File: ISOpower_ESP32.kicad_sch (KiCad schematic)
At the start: 23 parts, among them J10 ESPpin1-4, J2 SDI/SDO, J4 ESP-gpio-B, J5 1-pin-edge-touch-XL, J6 Touch Pins, J7 DAC/ADC, J9 i2c-header, U2 AMS1117-3.3, U3 ESP32-WROOM-32

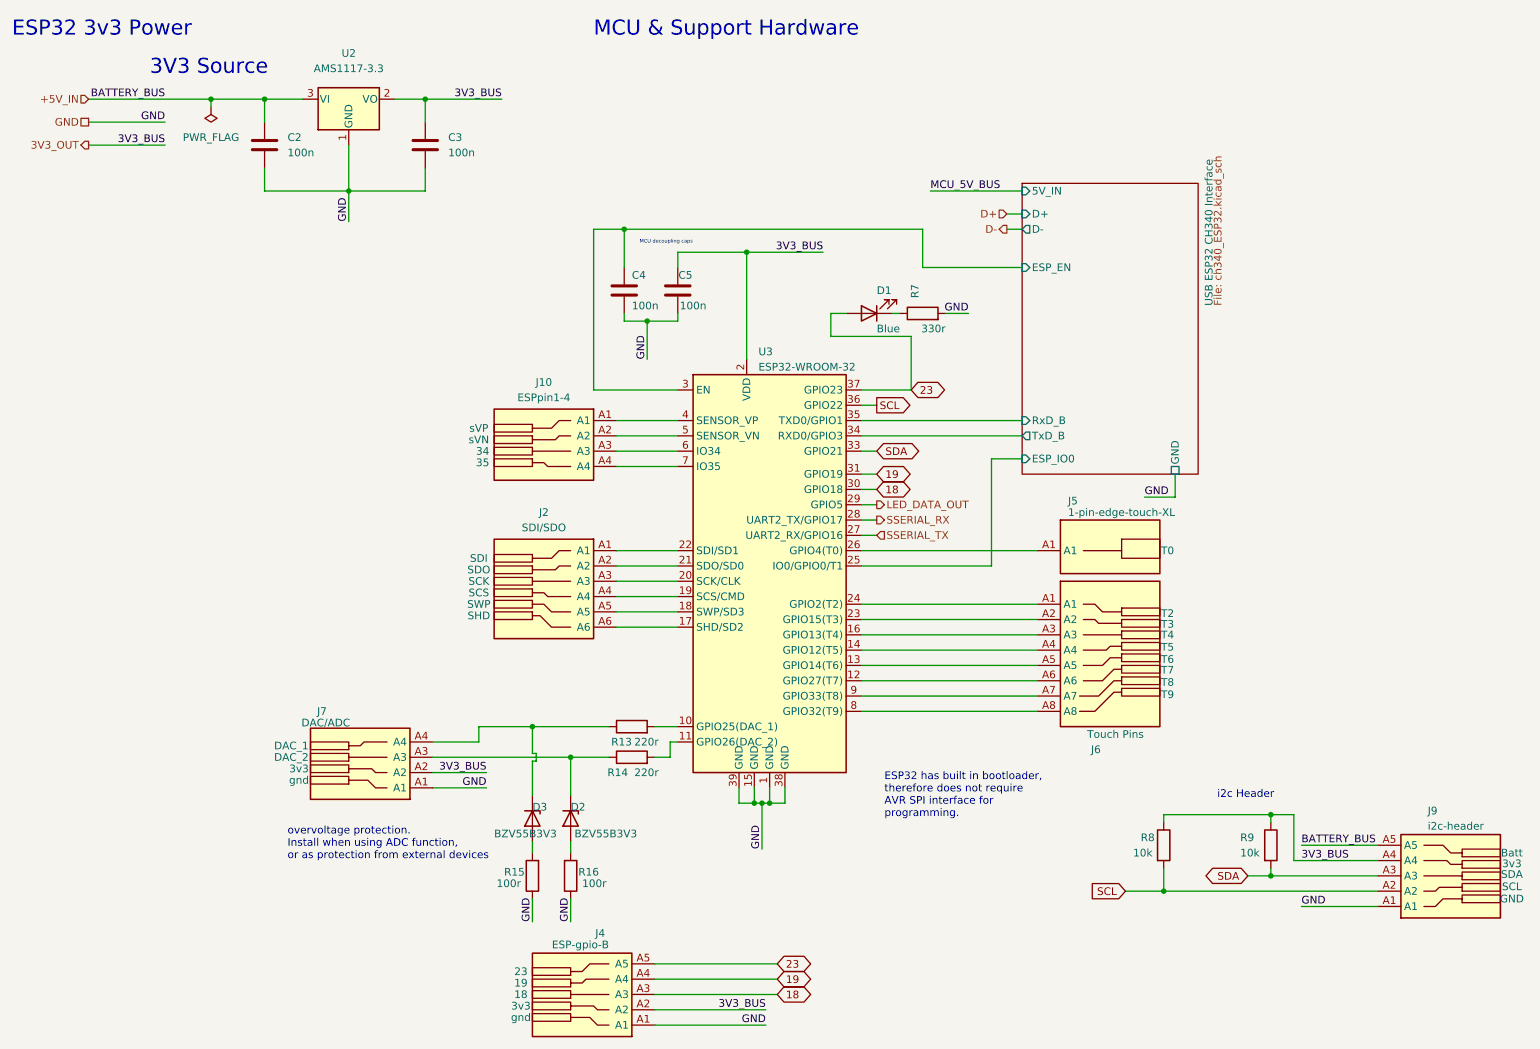
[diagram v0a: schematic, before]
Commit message: Got to Routing. Keeps crashing on me
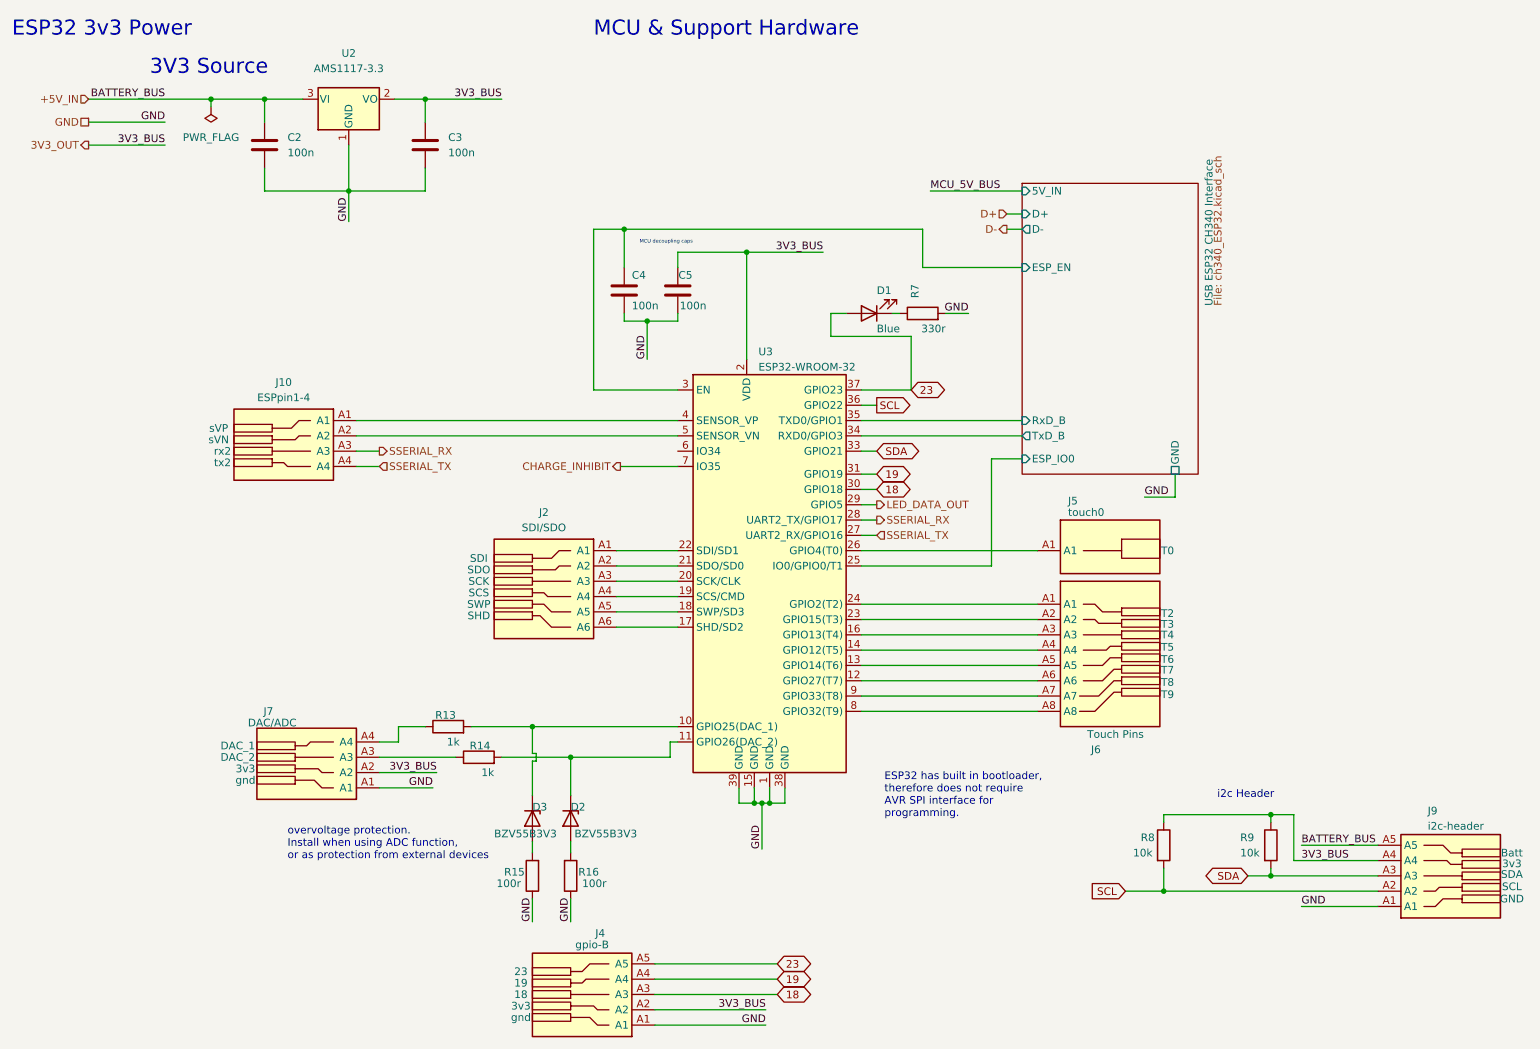
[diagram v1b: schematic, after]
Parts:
- J10: PIN3 34 -> rx2; PIN4 35 -> tx2
- J4: value ESP-gpio-B -> gpio-B
- J5: value 1-pin-edge-touch-XL -> touch0
- R13, R14: value 220r -> 1k
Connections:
- net SSERIAL_RX: now also J10.A3
- net SSERIAL_TX: now also J10.A4
- net at J7.A3, R14.1: no longer D2.1 (K)
- net at R13.2, U3.10 (GPIO25(DAC_1)): now also D3.1 (K)
- net at R14.2, U3.11 (GPIO26(DAC_2)): now also D2.1 (K)
- net at U3.6 (IO34): no longer J10.A3
- net CHARGE_INHIBIT: now reaches U3.7 (IO35)
- net CHARGE_INHIBIT: no longer J10.A4
- net at J7.A4, R13.1: no longer D3.1 (K)
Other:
- moved on the sheet: J10, J7, R13, R14

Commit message: Recoverd
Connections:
- net CHARGE_STATUS: now reaches U3.6 (IO34)
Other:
- note added: "#TODO: check voltage on these pins a and also function!"
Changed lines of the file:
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@@
     (stroke (width 0) (type default))
   )
-  (wire (pts (xy 116.205 88.9) (xy 125.73 88.9))
+  (wire (pts (xy 116.84 88.9) (xy 125.73 88.9))
     (stroke (width 0) (type default))
   )
@@
   )
   (wire (pts (xy 224.155 147.955) (xy 224.155 146.685))
+    (stroke (width 0) (type default))
+  )
+  (wire (pts (xy 116.84 86.36) (xy 125.73 86.36))
     (stroke (width 0) (type default))
   )
@@
     (effects (font (size 1.27 1.27)) (justify left bottom))
   )
+  (text "#TODO: check voltage on these pins a\nand also function!"
+    (at 86.36 95.25 0)
+    (effects (font (size 1.27 1.27)) (justify left bottom))
+  )
   (text "3V3 Source" (at 38.1 24.13 0)
     (effects (font (size 2.5 2.5)) (justify left bottom))
@@
     (effects (font (size 1.27 1.27)) (justify left))
   )
-  (hierarchical_label "CHARGE_INHIBIT" (shape output) (at 116.205 88.9 180) (fields_autoplaced)
+  (hierarchical_label "CHARGE_INHIBIT" (shape output) (at 116.84 88.9 180) (fields_autoplaced)
     (effects (font (size 1.27 1.27)) (justify right))
   )
@@
     (effects (font (size 1.27 1.27)) (justify right))
   )
+  (hierarchical_label "CHARGE_STATUS" (shape input) (at 116.84 86.36 180) (fields_autoplaced)
+    (effects (font (size 1.27 1.27)) (justify right))
+  )

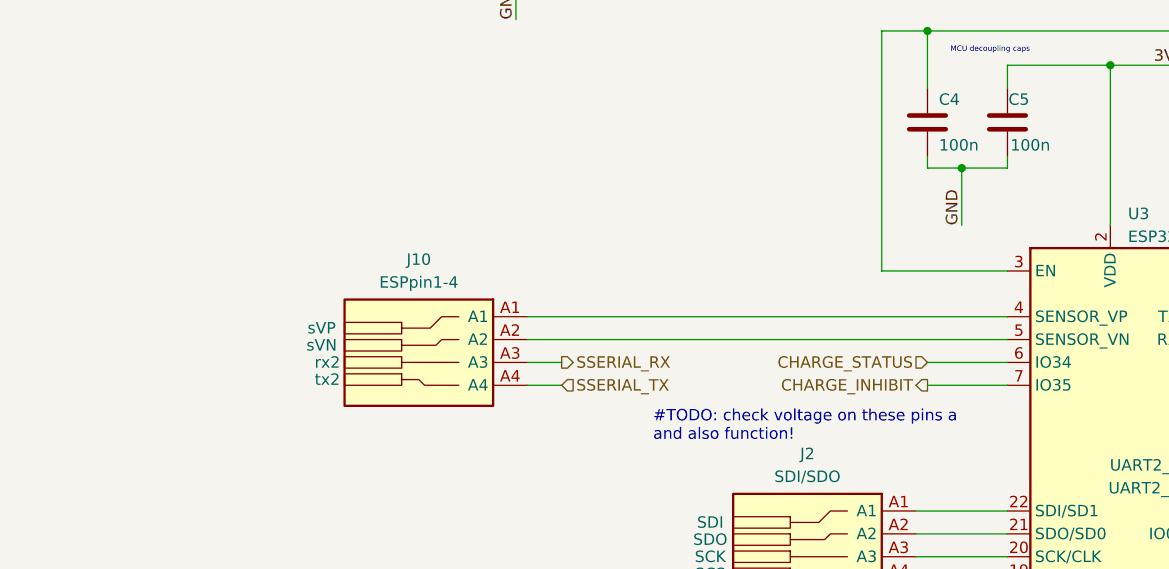
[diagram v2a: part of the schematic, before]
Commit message: Updated Schematic for Battery Charge Sense + read datasheet for battery charger IC
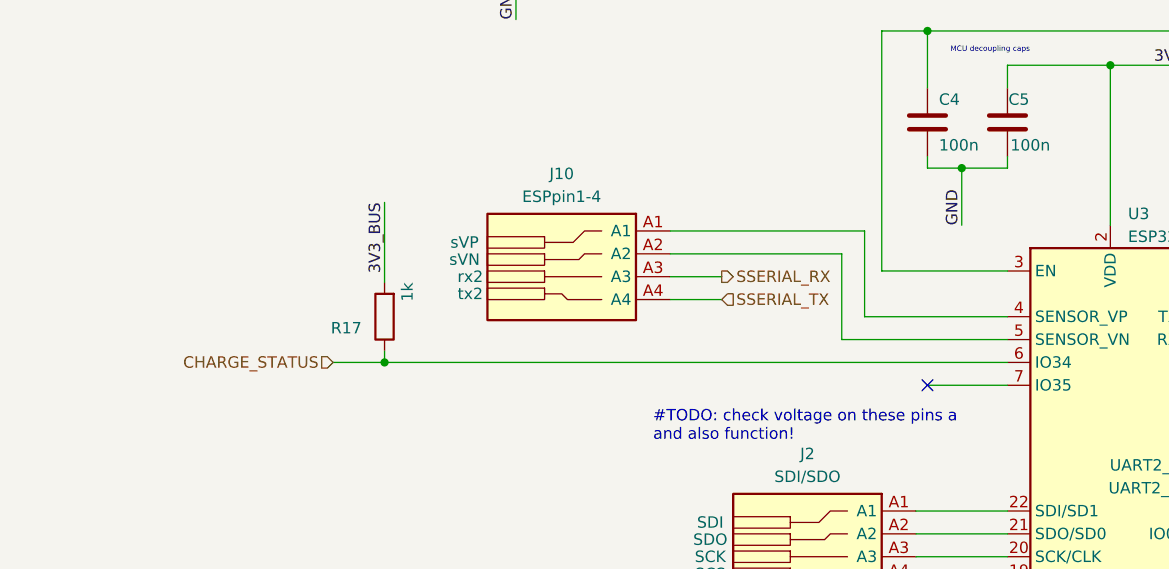
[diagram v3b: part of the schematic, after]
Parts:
- added R17: 1k, Resistor_SMD:R_0805_2012Metric_Pad1.20x1.40mm_HandSolder, symbol 000_Resistors_Immo:Resistor_0805
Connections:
- net 3V3_OUT: now also R17.2
- net CHARGE_STATUS: now also R17.1
- net CHARGE_INHIBIT: no longer names the net of U3.7 (IO35)
- no-connect marks 0 -> 1
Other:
- moved on the sheet: J10
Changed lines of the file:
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@@
   (junction (at 224.155 146.685) (diameter 0) (color 0 0 0 0)
   )
+  (junction (at 56.515 86.36) (diameter 0) (color 0 0 0 0)
+  )
   (junction (at 107.95 137.16) (diameter 0) (color 0 0 0 0)
   )
@@
   (junction (at 101.6 132.08) (diameter 0) (color 0 0 0 0)
   )
+  (no_connect (at 116.84 88.9))
   (wire (pts (xy 115.57 115.57) (xy 125.73 115.57))
     (stroke (width 0) (type default))
@@
     (stroke (width 0) (type default))
   )
-  (wire (pts (xy 72.39 88.9) (xy 76.2 88.9))
+  (wire (pts (xy 88.265 79.375) (xy 93.98 79.375))
     (stroke (width 0) (type default))
   )
@@
     (stroke (width 0) (type default))
   )
+  (wire (pts (xy 56.515 85.09) (xy 56.515 86.36))
+    (stroke (width 0) (type default))
+  )
   (wire (pts (xy 101.6 143.51) (xy 101.6 137.795))
     (stroke (width 0) (type default))
@@
     (stroke (width 0) (type default))
   )
+  (wire (pts (xy 88.265 71.755) (xy 109.855 71.755))
+    (stroke (width 0) (type default))
+  )
   (wire (pts (xy 140.97 144.78) (xy 143.51 144.78))
     (stroke (width 0) (type default))
@@
     (stroke (width 0) (type default))
   )
+  (wire (pts (xy 88.265 74.295) (xy 107.315 74.295))
+    (stroke (width 0) (type default))
+  )
   (wire (pts (xy 227.965 154.305) (xy 241.935 154.305))
     (stroke (width 0) (type default))
   )
-  (wire (pts (xy 72.39 81.28) (xy 125.73 81.28))
+  (wire (pts (xy 107.315 83.82) (xy 125.73 83.82))
     (stroke (width 0) (type default))
   )
@@
     (stroke (width 0) (type default))
   )
+  (wire (pts (xy 56.515 86.36) (xy 125.73 86.36))
+    (stroke (width 0) (type default))
+  )
   (wire (pts (xy 156.21 116.84) (xy 185.42 116.84))
     (stroke (width 0) (type default))
@@
     (stroke (width 0) (type default))
   )
-  (wire (pts (xy 72.39 86.36) (xy 76.2 86.36))
+  (wire (pts (xy 88.265 76.835) (xy 93.98 76.835))
     (stroke (width 0) (type default))
   )
@@
     (stroke (width 0) (type default))
   )
+  (wire (pts (xy 109.855 81.28) (xy 109.855 71.755))
+    (stroke (width 0) (type default))
+  )
   (wire (pts (xy 83.82 27.94) (xy 96.52 27.94))
     (stroke (width 0) (type default))
@@
     (stroke (width 0) (type default))
   )
+  (wire (pts (xy 109.855 81.28) (xy 125.73 81.28))
+    (stroke (width 0) (type default))
+  )
   (wire (pts (xy 177.8 87.63) (xy 182.88 87.63))
     (stroke (width 0) (type default))
@@
     (stroke (width 0) (type default))
   )
+  (wire (pts (xy 56.515 68.58) (xy 56.515 77.47))
+    (stroke (width 0) (type default))
+  )
   (wire (pts (xy 220.345 156.845) (xy 224.155 156.845))
     (stroke (width 0) (type default))
@@
     (stroke (width 0) (type default))
   )
+  (wire (pts (xy 107.315 74.295) (xy 107.315 83.82))
+    (stroke (width 0) (type default))
+  )
   (wire (pts (xy 91.44 132.08) (xy 101.6 132.08))
     (stroke (width 0) (type default))
@@
     (stroke (width 0) (type default))
   )
-  (wire (pts (xy 116.84 86.36) (xy 125.73 86.36))
+  (wire (pts (xy 50.8 86.36) (xy 56.515 86.36))
     (stroke (width 0) (type default))
   )
@@
   )
   (wire (pts (xy 116.84 49.53) (xy 116.84 55.88))
-    (stroke (width 0) (type default))
-  )
-  (wire (pts (xy 72.39 83.82) (xy 125.73 83.82))
     (stroke (width 0) (type default))
   )
@@
   )
   (label "GND" (at 85.09 142.24 180) (fields_autoplaced)
+    (effects (font (size 1.27 1.27)) (justify right bottom))
+  )
+  (label "3V3_BUS" (at 56.515 68.58 270) (fields_autoplaced)
     (effects (font (size 1.27 1.27)) (justify right bottom))
   )
@@
     (effects (font (size 1.27 1.27)) (justify left))
   )
-  (hierarchical_label "CHARGE_INHIBIT" (shape output) (at 116.84 88.9 180) (fields_autoplaced)
-    (effects (font (size 1.27 1.27)) (justify right))
-  )
   (hierarchical_label "D+" (shape input) (at 180.34 46.99 180) (fields_autoplaced)
     (effects (font (size 1.27 1.27)) (justify right))
@@
     (effects (font (size 1.27 1.27)) (justify right))
   )
-  (hierarchical_label "CHARGE_STATUS" (shape input) (at 116.84 86.36 180) (fields_autoplaced)
+  (hierarchical_label "CHARGE_STATUS" (shape input) (at 50.8 86.36 180) (fields_autoplaced)
     (effects (font (size 1.27 1.27)) (justify right))
   )
@@
     (effects (font (size 1.27 1.27)) (justify right))
   )
-  (hierarchical_label "SSERIAL_RX" (shape output) (at 76.2 86.36 0) (fields_autoplaced)
+  (hierarchical_label "SSERIAL_RX" (shape output) (at 93.98 76.835 0) (fields_autoplaced)
     (effects (font (size 1.27 1.27)) (justify left))
   )
@@
     (effects (font (size 1.27 1.27)) (justify left))
   )
-  (hierarchical_label "SSERIAL_TX" (shape input) (at 76.2 88.9 0) (fields_autoplaced)
+  (hierarchical_label "SSERIAL_TX" (shape input) (at 93.98 79.375 0) (fields_autoplaced)
     (effects (font (size 1.27 1.27)) (justify left))
   )
@@
     )
   )
-  (symbol (lib_id "000-edge-connectors-immo:4-pin-edge-touch") (at 57.15 96.52 0) (mirror y) (unit 1)
-    (in_bom yes) (on_board yes) (dnp no)
-    (property "Reference" "J10" (at 60.325 74.93 0)
-      (effects (font (size 1.27 1.27)))
-    )
-    (property "Value" "ESPpin1-4" (at 60.325 77.47 0)
-      (effects (font (size 1.27 1.27)))
-    )
-    (property "Footprint" "000-edge-connectors-immo:4-pin-edge" (at 72.39 135.89 0)
-      (effects (font (size 1.27 1.27)) hide)
-    )
-    (property "Datasheet" "http://www.ritrontek.com/uploadfile/2016/1026/20161026105231124.pdf#page=63" (at 53.34 124.46 0)
-      (effects (font (size 1.27 1.27)) hide)
-    )
-    (property "PIN1" "sVP" (at 49.53 82.55 0)
-      (effects (font (size 1.27 1.27)))
-    )
-    (property "PIN2" "sVN" (at 49.53 84.455 0)
-      (effects (font (size 1.27 1.27)))
-    )
-    (property "PIN3" "rx2" (at 50.165 86.36 0)
-      (effects (font (size 1.27 1.27)))
-    )
-    (property "PIN4" "tx2" (at 50.165 88.265 0)
+  (symbol (lib_id "000-edge-connectors-immo:4-pin-edge-touch") (at 73.025 86.995 0) (mirror y) (unit 1)
+    (in_bom yes) (on_board yes) (dnp no)
+    (property "Reference" "J10" (at 76.2 65.405 0)
+      (effects (font (size 1.27 1.27)))
+    )
+    (property "Value" "ESPpin1-4" (at 76.2 67.945 0)
+      (effects (font (size 1.27 1.27)))
+    )
+    (property "Footprint" "000-edge-connectors-immo:4-pin-edge" (at 88.265 126.365 0)
+      (effects (font (size 1.27 1.27)) hide)
+    )
+    (property "Datasheet" "http://www.ritrontek.com/uploadfile/2016/1026/20161026105231124.pdf#page=63" (at 69.215 114.935 0)
+      (effects (font (size 1.27 1.27)) hide)
+    )
+    (property "PIN1" "sVP" (at 65.405 73.025 0)
+      (effects (font (size 1.27 1.27)))
+    )
+    (property "PIN2" "sVN" (at 65.405 74.93 0)
+      (effects (font (size 1.27 1.27)))
+    )
+    (property "PIN3" "rx2" (at 66.04 76.835 0)
+      (effects (font (size 1.27 1.27)))
+    )
+    (property "PIN4" "tx2" (at 66.04 78.74 0)
       (effects (font (size 1.27 1.27)))
     )
@@
         )
       )
+    )
+  )
+  (symbol (lib_id "000_Resistors_Immo:Resistor_0805") (at 56.515 81.28 180) (unit 1)
+    (in_bom yes) (on_board yes) (dnp no)
+    (property "Reference" "R17" (at 53.975 82.5501 0)
+      (effects (font (size 1.27 1.27)) (justify left))
+    )
+    (property "Value" "1k" (at 59.055 77.47 90)
+      (effects (font (size 1.27 1.27)) (justify left))
+    )
+    (property "Footprint" "Resistor_SMD:R_0805_2012Metric_Pad1.20x1.40mm_HandSolder" (at 58.293 81.28 90)
+      (effects (font (size 1.27 1.27)) hide)
+    )
+    (property "Datasheet" "~" (at 56.515 81.28 0)
+      (effects (font (size 1.27 1.27)) hide)
+    )
+    (pin "1")
+    (pin "2")
+    (instances
+      (project "ImogenWren"
+        (path "/84b7ad53-68b5-40da-9777-f5bb9a09ecb4/9cdb06a8-babb-4d9b-a75e-e6e2cfc518a0"
+          (reference "R17") (unit 1)
+        )
+      )
